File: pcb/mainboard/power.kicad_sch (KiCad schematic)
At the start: 135 parts, among them J1 Conn_01x10_MountingPin, Q1 FDMC8327L, Q2 FDMC8327L, Q3 2SK3018, U1 SY8120, U10 XC6206P122MR, U101 MCIMX7S5EVM08SC, U2 SY8120, U3 SY8120, U4 SY8120, U5 SY8120, U6 SY8120, U7 LT8606, U8 LTC4162-F, U9 ADP123

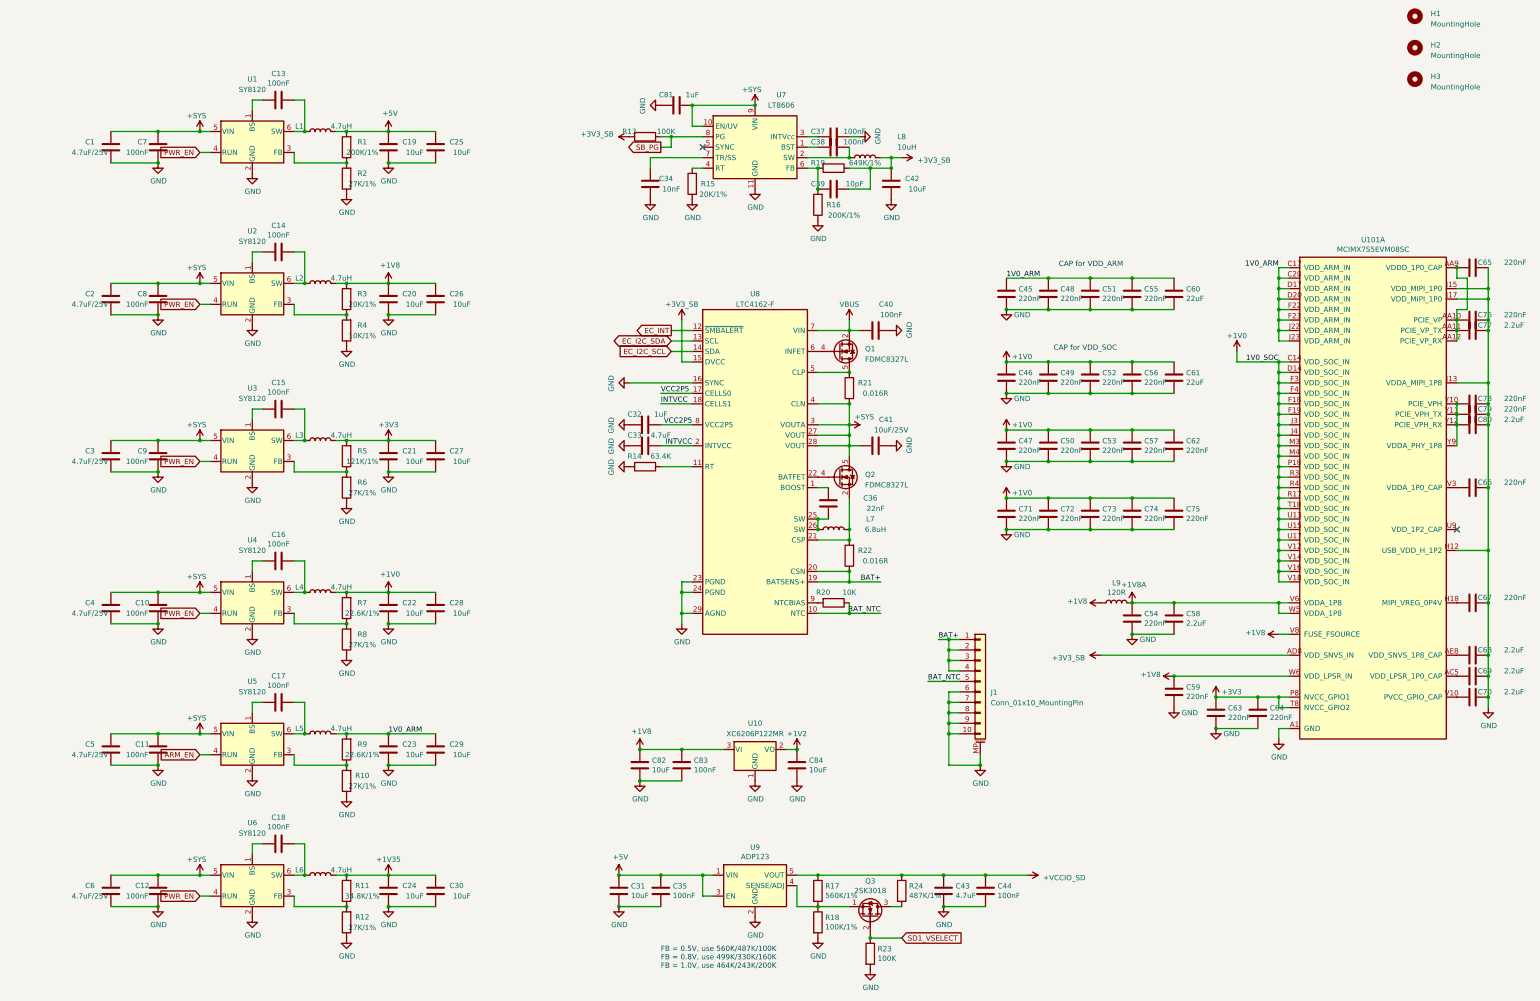
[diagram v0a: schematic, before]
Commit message: pcb: preliminary r0p1 schematics
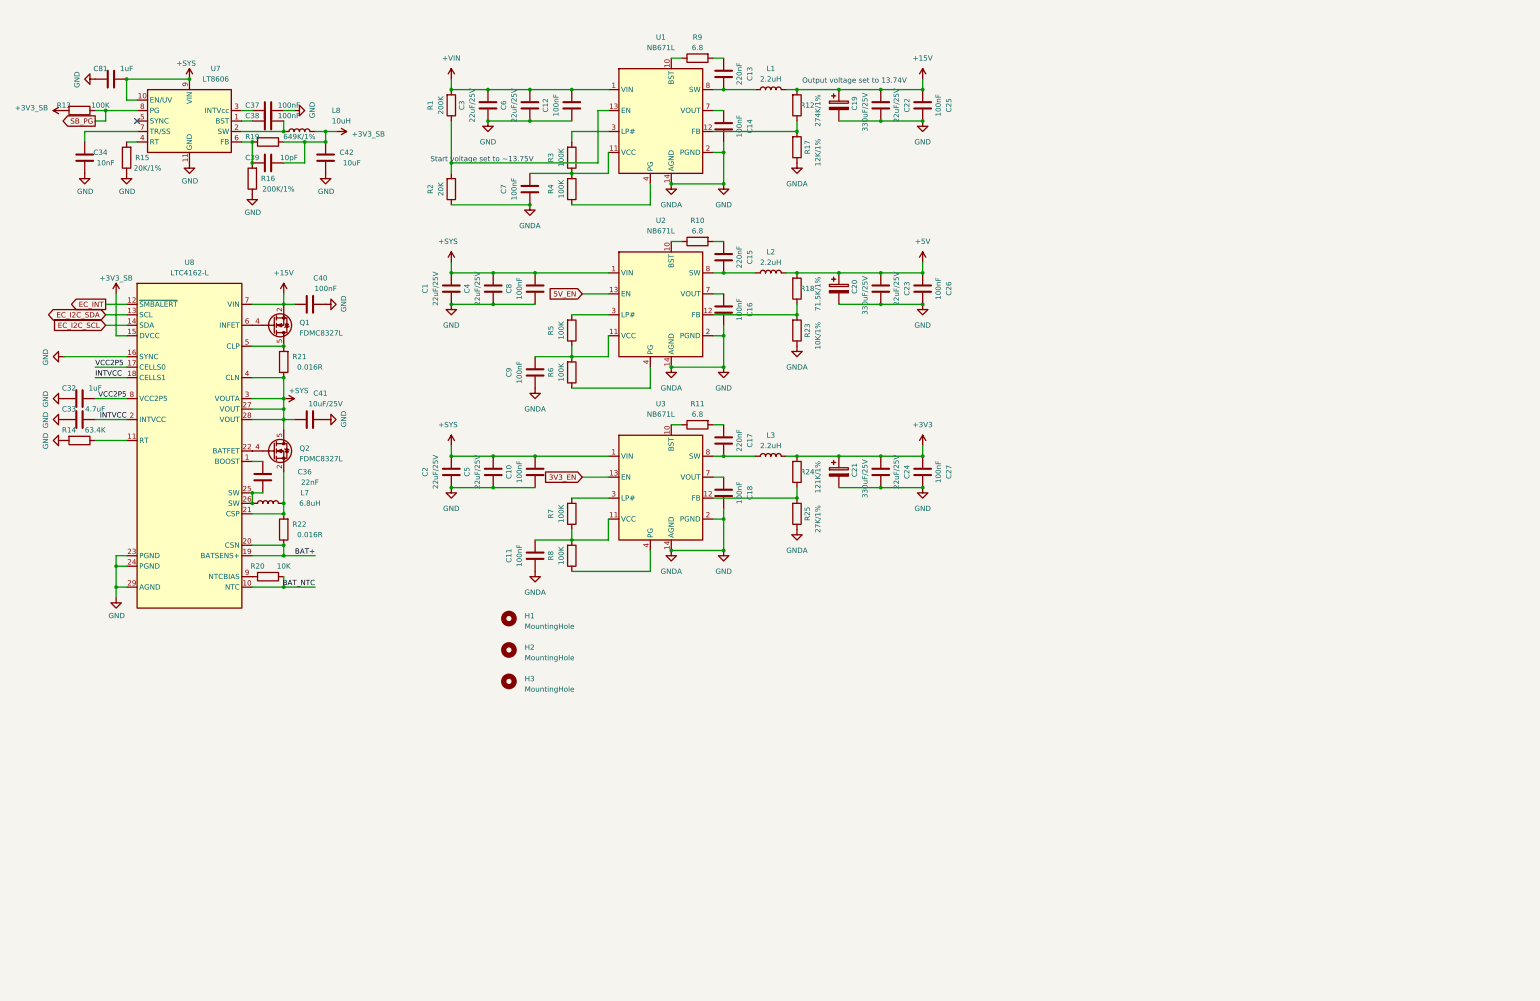
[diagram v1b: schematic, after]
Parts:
- removed C19, C20, C21, C28, C29, C30, C31, C82, C84: 10uF, Capacitor_SMD:C_0603_1608Metric, symbol Device:C
- removed C35, C44, C83: 100nF, Capacitor_SMD:C_0402_1005Metric, symbol Device:C
- removed C43: 4.7uF, Capacitor_SMD:C_0603_1608Metric, symbol Device:C
- removed C45, C46, C47, C48, C49, C50, C51, C52, C53, C54, C55, C56, C57, C59, C62, C63, C64, C65, C66, C67, C71, C72, C73, C74, C75, C76, C78, C79: 220nF, Capacitor_SMD:C_0402_1005Metric, symbol Device:C
- removed C58, C68, C69, C70, C77, C80: 2.2uF, Capacitor_SMD:C_0402_1005Metric, symbol Device:C
- removed C60, C61: 22uF, Capacitor_SMD:C_0603_1608Metric, symbol Device:C
- removed J1: Conn_01x10_MountingPin, Connector_FFC-FPC:Hirose_FH12-10S-0.5SH_1x10-1MP_P0.50mm_Horizontal, symbol Connector_Generic_MountingPin:Conn_01x10_MountingPin
- removed L4, L5, L6: 4.7uH, Inductor_SMD:L_Vishay_IHLP-1212, symbol Device:L
- removed L9: 120R, Inductor_SMD:L_0603_1608Metric, symbol Device:L
- removed Q3: 2SK3018, Package_TO_SOT_SMD:SOT-23, symbol Device:Q_NMOS_SGD
- removed U1, U2, U3, U4, U5, U6: SY8120, Package_TO_SOT_SMD:TSOT-23-6, symbol symbols:SY8120
- removed U10: XC6206P122MR, Package_TO_SOT_SMD:SOT-23, symbol Regulator_Linear:XC6206PxxxMR
- removed U101: MCIMX7S5EVM08SC, footprints:BGA-541_25x25_19.0x19.0mm, symbol symbols:MCIMX7S5EVM08SC
- removed U9: ADP123, Package_TO_SOT_SMD:TSOT-23-5, symbol Regulator_Linear:ADP7142AUJZ
- added C19, C20, C21: 330uF/25V, symbol Device:C_Polarized
- added R25: 27K/1%, Resistor_SMD:R_0402_1005Metric, symbol Device:R
- added U1, U2, U3: NB671L, footprints:MPS_QFN-16_3x3mm_P0.4mm, symbol symbols:NB671L
- C1, C2, C3, C4, C5, C6: value 4.7uF/25V -> 22uF/25V; footprint Capacitor_SMD:C_0805_2012Metric -> Capacitor_SMD:C_1206_3216Metric
- C13, C15, C17: value 100nF -> 220nF
- C22, C23, C24: value 10uF -> 22uF/25V; footprint Capacitor_SMD:C_0603_1608Metric -> Capacitor_SMD:C_1206_3216Metric
- C25, C26, C27: value 10uF -> 100nF; footprint Capacitor_SMD:C_0603_1608Metric -> Capacitor_SMD:C_0402_1005Metric
- L1, L2, L3: value 4.7uH -> 2.2uH
- R1: value 200K/1% -> 200K
- R10: value 27K/1% -> 6.8
- R11: value 34.8K/1% -> 6.8
- R12: value 27K/1% -> 274K/1%
- R17: value 560K/1% -> 12K/1%
- R18: value 100K/1% -> 71.5K/1%
- R2: value 27K/1% -> 20K
- R23: value 100K -> 10K/1%
- R24: value 487K/1% -> 121K/1%
- R3: value 20K/1% -> 100K
- R4: value 10K/1% -> 100K
- R5: value 121K/1% -> 100K
- R6, R8: value 27K/1% -> 100K
- R7: value 22.6K/1% -> 100K
- R9: value 22.6K/1% -> 6.8
- U8: value LTC4162-F -> LTC4162-L
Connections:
- net SD1_VSELECT is gone; now on net GND: R23.1
- net +3V3: now also C24.1, C27.1, R24.2, C21.1; no longer C27.2, R5.2
- net +5V: now also C23.1, C26.1, L2.2, R18.2, C20.1; no longer C25.2, L1.2, R1.2
- net +SYS: now also C1.1, C10.1, C2.1, C4.1, C5.1, C8.1, U2.1 (VIN), U3.1 (VIN); no longer C1.2, C10.2, C11.2, C12.2, C2.2, C3.2, C4.2, C5.2, C6.2, C7.2, C8.2, C9.2
- net GND: now also C1.2, C10.2, C11.2, C12.2, C14.2, C16.2, C18.2, C2.2, C22.2, C23.2, C24.2, C25.2, C26.2, C27.2, C3.2, C4.2, C5.2, C6.2, C7.2, C8.2, C9.2, R17.1, C19.2, C20.2, C21.2, R25.1, U1.14 (AGND), U1.2 (PGND), U2.14 (AGND), U2.2 (PGND), U3.14 (AGND), U3.2 (PGND); no longer C1.1, C10.1, C11.1, C12.1, C2.1, C22.1, C23.1, C24.1, C25.1, C26.1, C27.1, C3.1, C4.1, C5.1, C6.1, C7.1, C8.1, C9.1, R10.1, R12.1, R18.2, R23.2, R4.1, R6.1, R8.1
- net at C17.1: now also R11.2
- net at R5.1, R6.2: now also C9.1, U2.11 (VCC)
- net at R18.1: now also R23.2, U2.12 (FB); no longer R17.2
- net at R11.1: now also U3.10 (BST); no longer R12.2
- net at C18.1: now also U3.7 (VOUT)
- net at L2.1: now also C15.2, U2.15 (SW), U2.16 (SW), U2.8 (SW), U2.9 (SW); no longer C14.1
- net at L3.1: now also C17.2, U3.15 (SW), U3.16 (SW), U3.8 (SW), U3.9 (SW); no longer C15.1
- net at R1.1, R2.2: now also U1.13 (EN)
- net at R7.1, R8.2: now also C11.1, U3.11 (VCC)
- net at R9.1: now also U1.10 (BST); no longer R10.2
- net at C13.1: now also R9.2; no longer L1.1
- net at C16.1: now also U2.7 (VOUT)
- net at R3.1, R4.2: now also C7.1, U1.11 (VCC)
- net at C13.2: now also L1.1, U1.15 (SW), U1.16 (SW), U1.8 (SW), U1.9 (SW)
- net +1V0: no longer names the net of R7.2
- net +1V0: now also U3.3 (LP#); no longer C22.2
- removed net +1V35: C24.2, R11.2
- removed net +1V8: C26.2, L2.2, R3.2
- net +VCCIO_SD: no longer names the net of R24.1
- net +VCCIO_SD: now also R25.2, U3.12 (FB); no longer R17.1
- removed net 1V0_ARM: C23.2, R9.2
- net VBUS renamed +15V
- net +15V: now also C22.1, C25.1, L1.2, R12.2, C19.1
- new net: R4.1, U1.4 (PG)
- new net: R3.2, U1.3 (LP#)
- new net: R8.1, U3.4 (PG)
- new net: R5.2, U2.3 (LP#)
- new net: R6.1, U2.4 (PG)
- new net: C15.1, R10.2
- new net: R12.1, R17.2, U1.12 (FB)
- new net: C14.1, U1.7 (VOUT)
- new net: R10.1, U2.10 (BST)
- new net +VIN: C12.1, C3.1, C6.1, R1.2, U1.1 (VIN)
- new net 3V3_EN: U3.13 (EN)
- new net 5V_EN: U2.13 (EN)
- no-connect marks 2 -> 1
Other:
- note added: "Output voltage set to 13.74V"
- note added: "Start voltage set to ~13.75V"
- note removed: "CAP for VDD_ARM"
- note removed: "CAP for VDD_SOC"
- note removed: "FB = 0.5V, use 560K/487K/100K FB = 0.8V, use 499K/330K/160K FB = 1.0V, use 464K/243K/200K"
- company: Copyright EI-2030 2021. / Engineer: Wenting Zhang -> Copyright Modos 2021. / Engineer: Wenting Zhang
- moved on the sheet: C32, C33, C34, C36, C37, C38, C39, C40, C41, C42, C81, H1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

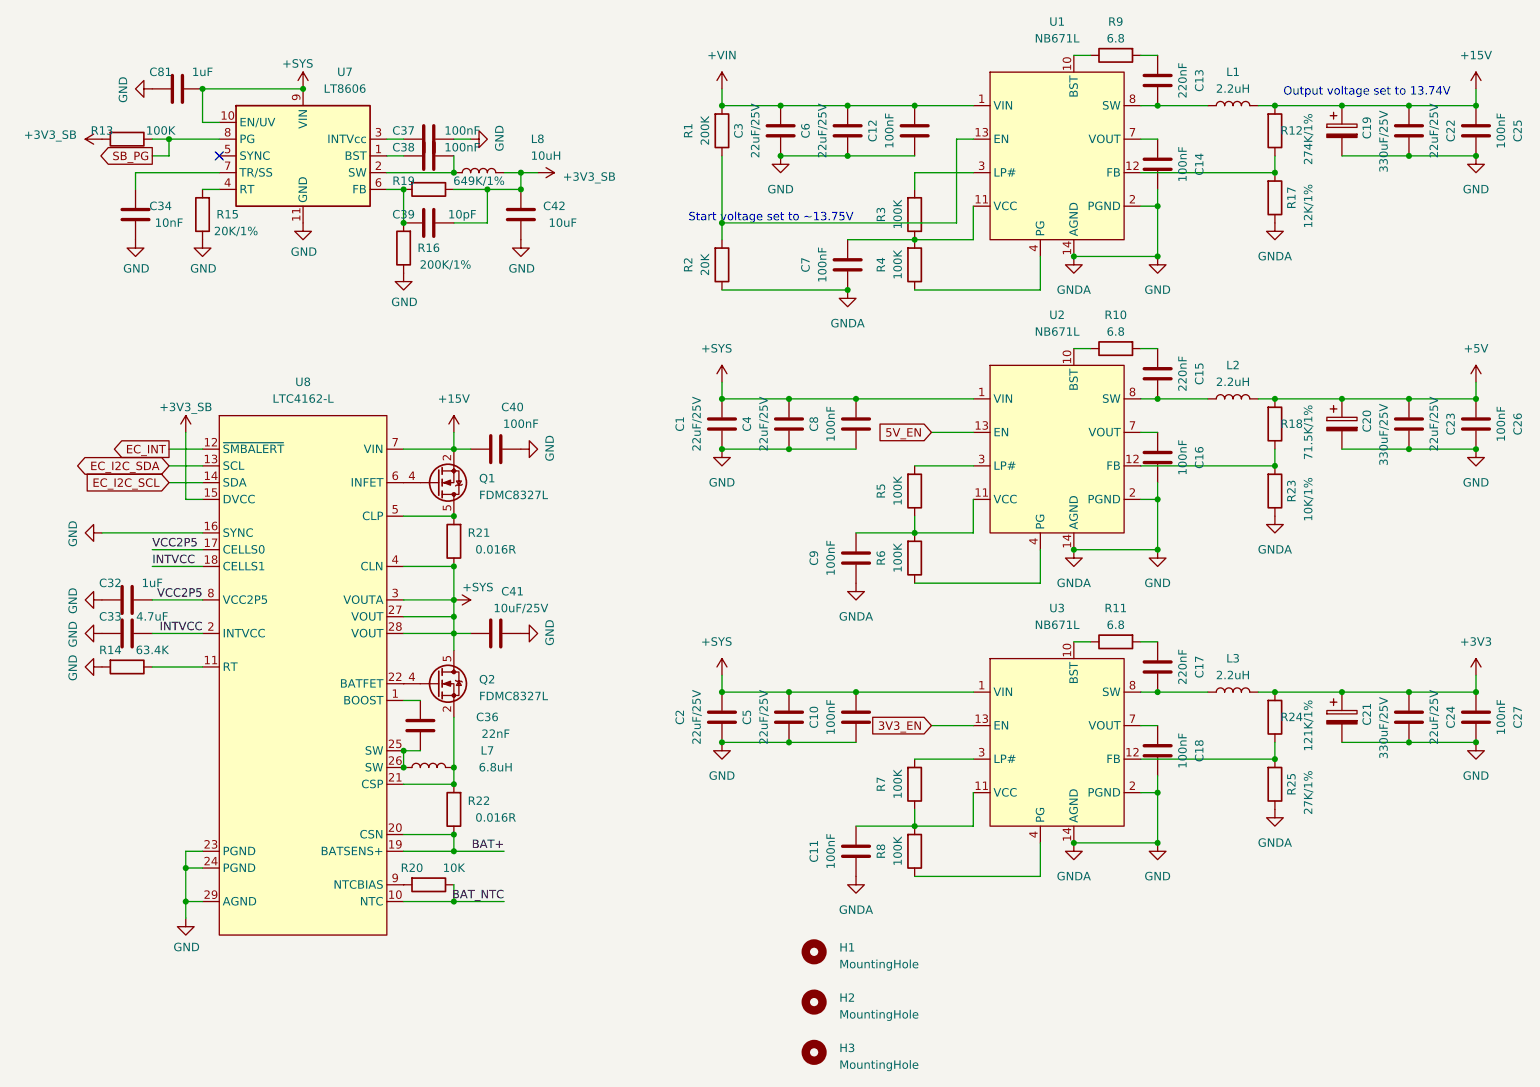
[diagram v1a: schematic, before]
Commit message: pcb: initial placement for mb
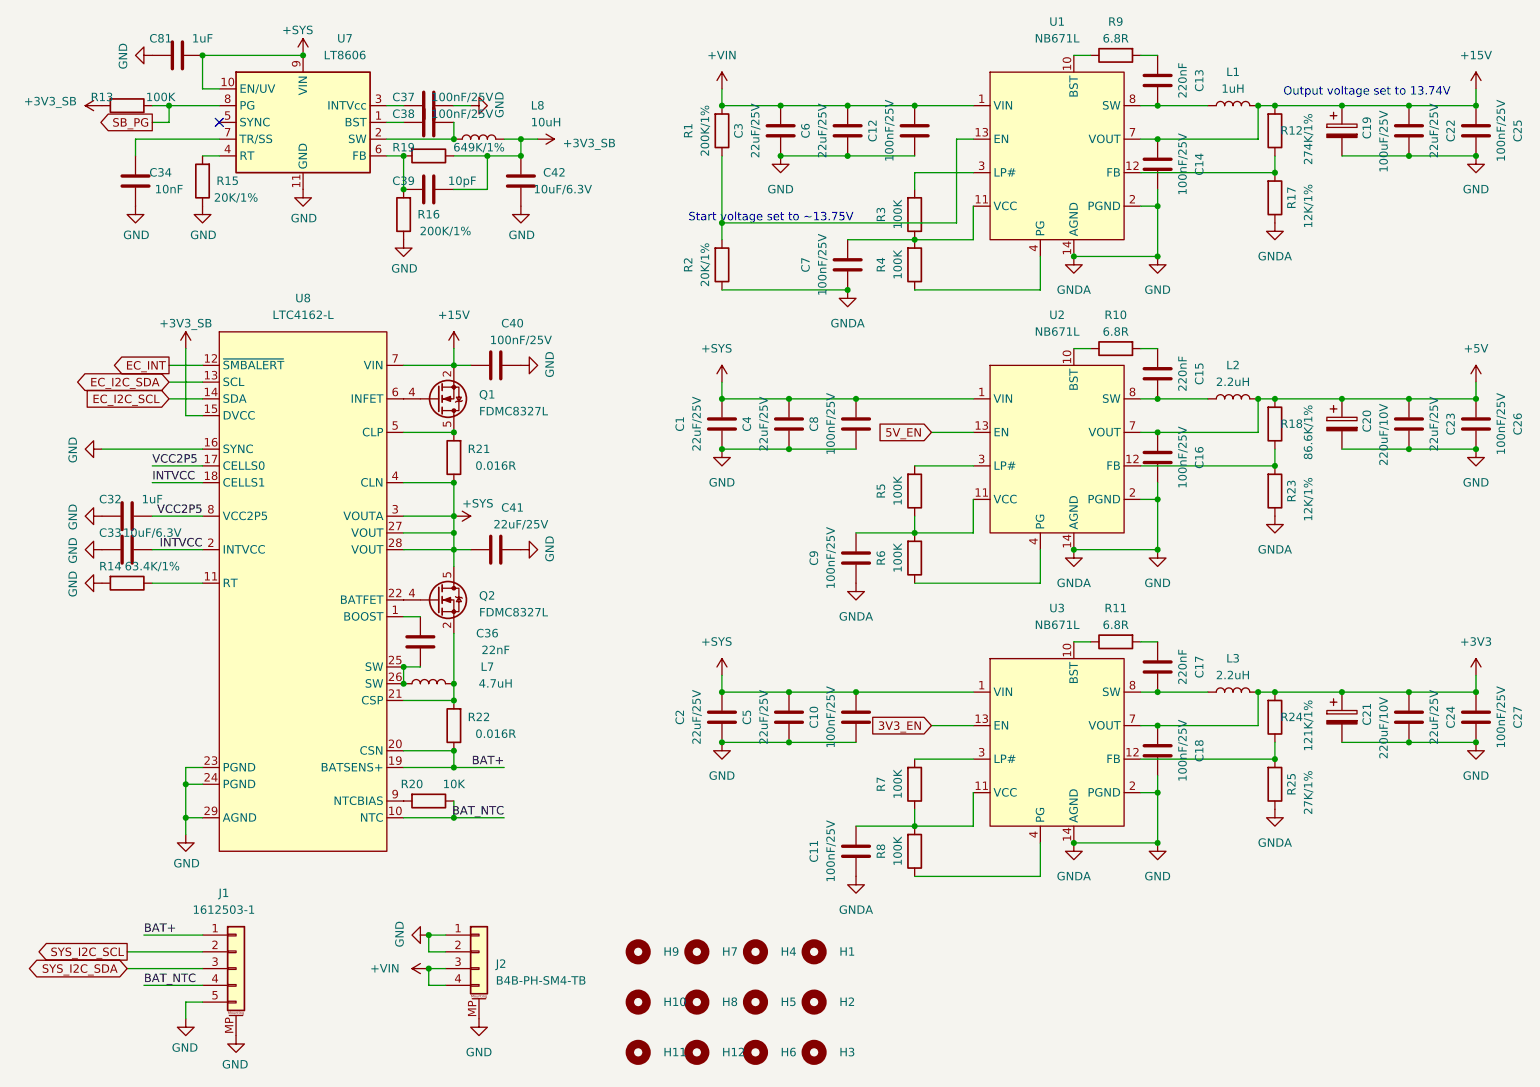
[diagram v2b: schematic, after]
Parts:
- added H10, H11, H9: MountingHole, MountingHole:MountingHole_3.7mm_Pad, symbol Mechanical:MountingHole
- added H12: MountingHole, MountingHole:MountingHole_2.7mm_Pad, symbol Mechanical:MountingHole
- added H4, H5, H6, H7, H8: MountingHole, MountingHole:MountingHole_2.5mm_Pad, symbol Mechanical:MountingHole
- added J1: 1612503-1, footprints:TE_1612503-1, symbol Connector_Generic_MountingPin:Conn_01x05_MountingPin
- added J2: B4B-PH-SM4-TB, Connector_JST:JST_PH_B4B-PH-SM4-TB_1x04-1MP_P2.00mm_Vertical, symbol Connector_Generic_MountingPin:Conn_01x04_MountingPin
- C1, C2, C22, C23, C24, C3, C4, C5, C6: footprint Capacitor_SMD:C_1206_3216Metric -> Capacitor_SMD:C_0805_2012Metric; LCSC (none) -> C116413; Ref.Price (none) -> 0.0585
- C10, C11, C12, C14, C16, C18, C25, C26, C27, C37, C38, C40, C7, C8, C9: value 100nF -> 100nF/25V; LCSC (none) -> C56392; Ref.Price (none) -> 0.0023
- C13, C15, C17: LCSC (none) -> C880414; Ref.Price (none) -> 0.0036
- C19: value 330uF/25V -> 100uF/25V; footprint (none) -> Capacitor_SMD:C_Elec_6.3x5.8; LCSC (none) -> C249959; Ref.Price (none) -> 0.1004
- C20, C21: value 330uF/25V -> 220uF/10V; footprint (none) -> Capacitor_SMD:C_Elec_6.3x5.8; LCSC (none) -> C116413; Ref.Price (none) -> 0.0389
- C32, C81: LCSC (none) -> C157353; Ref.Price (none) -> 0.0034
- C33: value 4.7uF -> 10uF/6.3V; LCSC (none) -> C105490; Ref.Price (none) -> 0.0165
- C34: LCSC (none) -> C1524; Ref.Price (none) -> 0.0013
- C36: LCSC (none) -> C284978; Ref.Price (none) -> 0.0025
- C39: LCSC (none) -> C285132; Ref.Price (none) -> 0.011
- C41: value 10uF/25V -> 22uF/25V; LCSC (none) -> C116413; Ref.Price (none) -> 0.0585
- C42: value 10uF -> 10uF/6.3V; LCSC (none) -> C105490; Ref.Price (none) -> 0.0165
- H1, H2, H3: footprint MountingHole:MountingHole_2.2mm_M2_DIN965 -> MountingHole:MountingHole_2.5mm_Pad; LCSC (none) -> -; Ref.Price (none) -> 0
- L1: value 2.2uH -> 1uH; footprint Inductor_SMD:L_Vishay_IHLP-1212 -> footprints:L_MAPM0630F; LCSC (none) -> C280920; Ref.Price (none) -> 0.1167
- L2, L3: footprint Inductor_SMD:L_Vishay_IHLP-1212 -> footprints:L_MAPM1040F; LCSC (none) -> C280935; Ref.Price (none) -> 0.0743
- L7: value 6.8uH -> 4.7uH; footprint Inductor_SMD:L_Vishay_IHLP-1212 -> footprints:L_MAPM0630F
- L8: footprint Inductor_SMD:L_Vishay_IHLP-1212 -> footprints:L_1212; LCSC (none) -> C340381; Ref.Price (none) -> 0.0643
- Q1, Q2: LCSC (none) -> FDMC8327LCT-ND; Ref.Price (none) -> 0.873
- R1: value 200K -> 200K/1%; LCSC (none) -> C114763; Ref.Price (none) -> 0.0008
- R10, R11, R9: value 6.8 -> 6.8R; LCSC (none) -> C137844; Ref.Price (none) -> 0.0009
- R12: LCSC (none) -> C185435; Ref.Price (none) -> 0.0009
- R13, R3, R4, R5, R6, R7, R8: LCSC (none) -> C106234; Ref.Price (none) -> 0.0006
- R14: value 63.4K -> 63.4K/1%; LCSC (none) -> C137949; Ref.Price (none) -> 0.0009
- R15: LCSC (none) -> C93942; Ref.Price (none) -> 0.0011
- R16: LCSC (none) -> C114763; Ref.Price (none) -> 0.0008
- R17: LCSC (none) -> C114760; Ref.Price (none) -> 0.0008
- R18: value 71.5K/1% -> 86.6K/1%; LCSC (none) -> C477807; Ref.Price (none) -> 0.0009
- R19: LCSC (none) -> C273690; Ref.Price (none) -> 0.0009
- R2: value 20K -> 20K/1%; LCSC (none) -> C93942; Ref.Price (none) -> 0.0011
- R20: LCSC (none) -> C60489; Ref.Price (none) -> 0.0006
- R21, R22: footprint Resistor_SMD:R_0402_1005Metric -> Resistor_SMD:R_1206_3216Metric; LCSC (none) -> C175760; Ref.Price (none) -> 0.0206
- R23: value 10K/1% -> 12K/1%; LCSC (none) -> C114760; Ref.Price (none) -> 0.0008
- R24: LCSC (none) -> C112303; Ref.Price (none) -> 0.001
- R25: LCSC (none) -> C138022; Ref.Price (none) -> 0.0029
- U1, U2, U3: LCSC (none) -> 1589-1344-1-ND; Ref.Price (none) -> 2.47
- U7: LCSC (none) -> LT8606EMSE#PBF-ND; Ref.Price (none) -> 2.87
- U8: LCSC (none) -> 505-LTC4162EUFD-L42#TRPBFCT-ND; Ref.Price (none) -> 6.105
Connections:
- net +15V: now also C14.1, U1.7 (VOUT)
- net +3V3: now also C18.1, U3.7 (VOUT)
- net +5V: now also C16.1, U2.7 (VOUT)
- net +VIN: now also J2.3 (Pin_3), J2.4 (Pin_4)
- net BAT+: now also J1.1 (Pin_1)
- net BAT_NTC: now also J1.4 (Pin_4)
- net GND: now also J1.5 (Pin_5), J1.MP (MountPin), J2.1 (Pin_1), J2.2 (Pin_2), J2.MP (MountPin)
- new net SYS_I2C_SCL: J1.2 (Pin_2)
- new net SYS_I2C_SDA: J1.3 (Pin_3)
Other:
- moved on the sheet: C32, C33, C34, C36, C37, C38, C39, C40, C41, C42, C81, L7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
